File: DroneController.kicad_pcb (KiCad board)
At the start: 4 copper layers, 55 x 55 mm, 74 parts, among them P1 USB_C_Plug, Q2 AO3400A, Q3 AO3400A, U1 ICM-42605, U2 W25Q16JVSS, U3 BMP280, U5 STM32F411, U6 L86-M33, U7 915MHz, U9 AP7361C-33E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

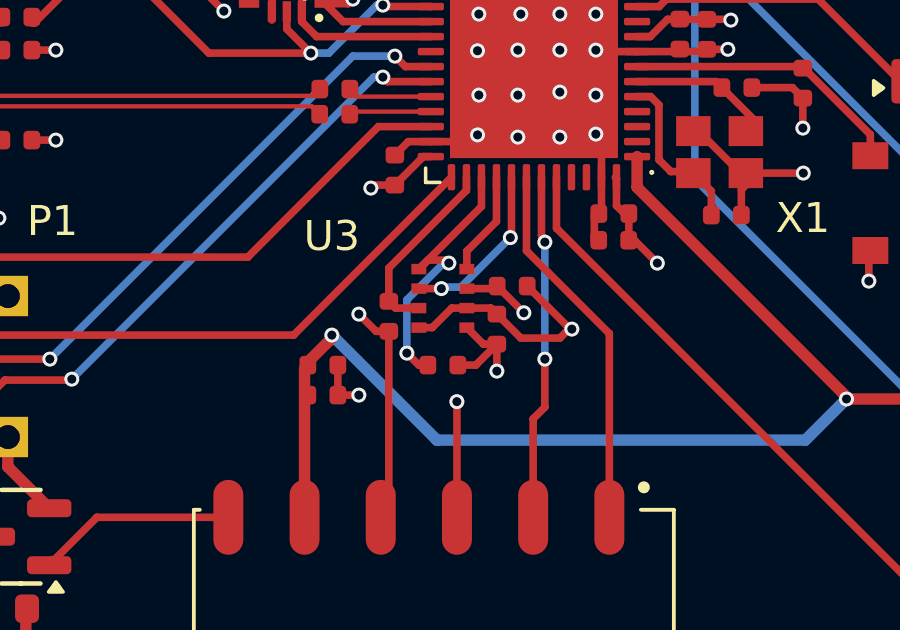
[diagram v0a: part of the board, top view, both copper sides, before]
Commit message: Modified BMP280 wiring, cleaned up schematic
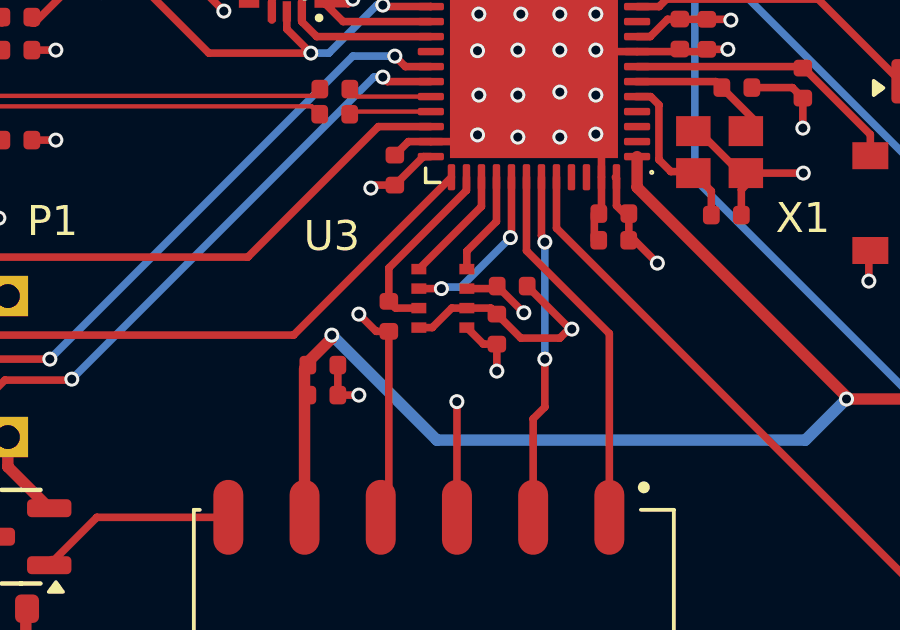
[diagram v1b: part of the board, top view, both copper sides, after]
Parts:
- removed R15: 5.1kΩ, PCM_JLCPCB:R_0402
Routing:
- net /SPI3_SCK: track 9.64 -> 3.93 mm, vias 2 -> 0
- net +3.3V: track 50.8 -> 49.2 mm
